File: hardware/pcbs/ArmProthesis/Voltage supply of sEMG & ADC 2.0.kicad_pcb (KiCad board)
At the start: 2 copper layers, 53 x 40 mm, 13 parts, among them U1 TLE2426CD, U2 LT1963AEQ

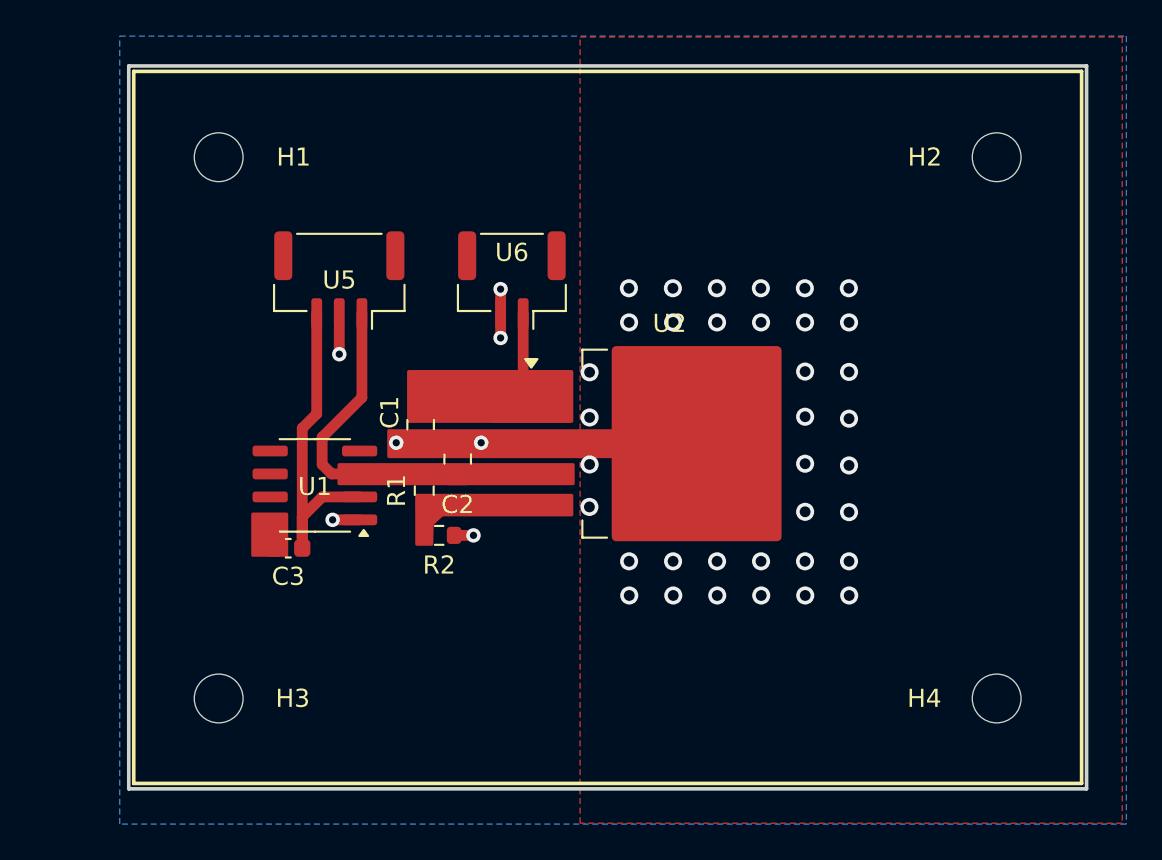
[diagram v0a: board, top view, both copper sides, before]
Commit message: new LDO with a proper rail splitter
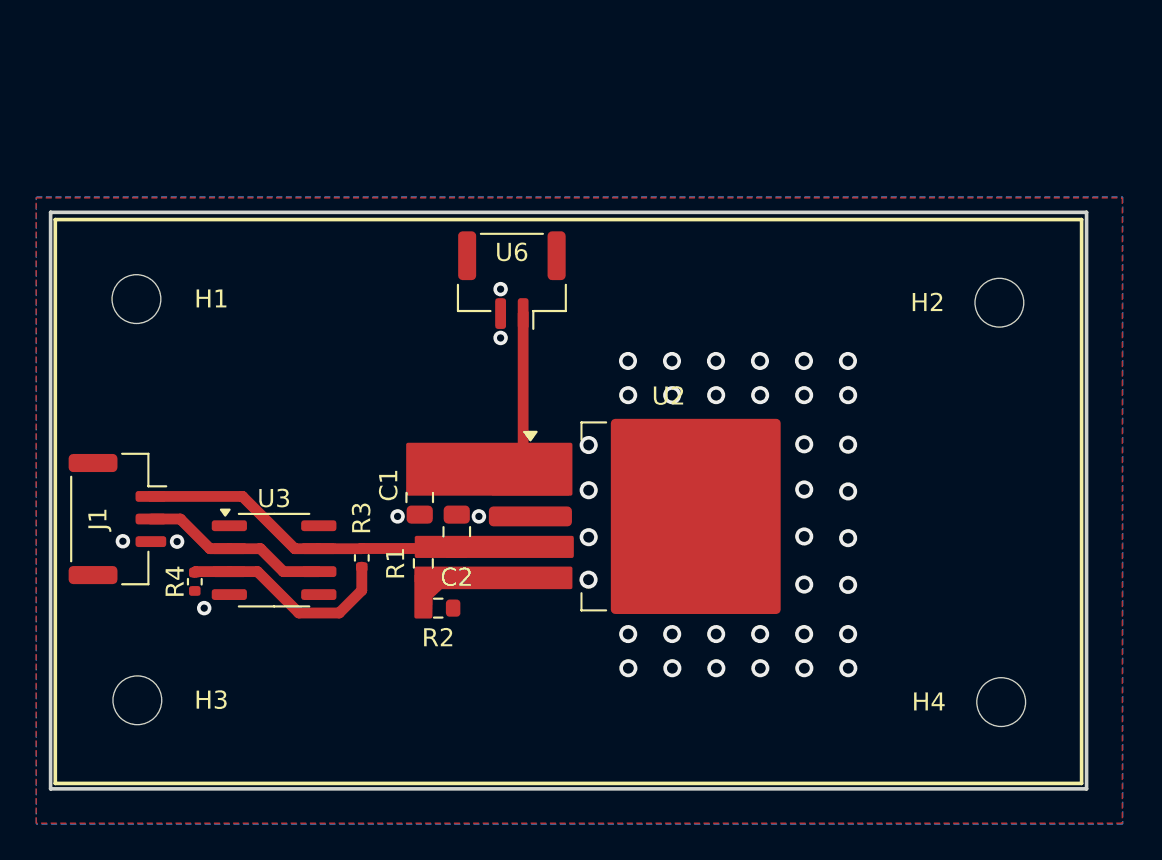
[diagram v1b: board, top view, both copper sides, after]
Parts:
- removed C3: 1uF, Capacitor_SMD:C_0603_1608Metric
- removed U1: TLE2426CD, Package_SO:SOIC-8_3.9x4.9mm_P1.27mm
- removed U5: ~, Connector_JST:JST_GH_SM03B-GHS-TB_1x03-1MP_P1.25mm_Horizontal
- added J1: Conn_01x03, Connector_JST:JST_GH_SM03B-GHS-TB_1x03-1MP_P1.25mm_Horizontal, F.Cu at (98.9, 71.2)
- added R3: 10k, Resistor_SMD:R_0402_1005Metric, F.Cu at (112.4, 73.3)
- added R4: 10k, Resistor_SMD:R_0402_1005Metric, F.Cu at (103.2, 74.6)
- added U3: OPA197xD, Package_SO:SOIC-8_3.9x4.9mm_P1.27mm, F.Cu at (107.6, 73.4)
- moved H1 9.07 mm to (100.0, 59.0)
- moved H2 8.05 mm to (147.7, 59.2)
- moved H3 4.50 mm to (100.0, 81.2)
- moved C2 4.03 mm to (117.7, 71.9)
- moved R1 4.03 mm to (115.8, 73.6)
- moved U2 4.03 mm to (129.4, 71.0)
- moved C1 4.03 mm to (115.6, 70.0)
- moved R2 4.03 mm to (116.7, 76.1)
- moved H4 0.32 mm to (147.8, 81.3)
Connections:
- net /+11.1V renamed 7.4V
- net /+5V renamed 5V
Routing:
- net /VGND: track 18.5 -> 0.00 mm
- net Net-(U3-+): track 0.00 -> 12.0 mm
- net 2.5V: track 0.00 -> 10.5 mm
- net GND: track 6.67 -> 0.00 mm
- net 7.4V: track 3.99 -> 8.63 mm
- net 5V: track 12.7 -> 16.3 mm
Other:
- board size 53 x 40 mm -> 57.3 x 31.9 mm

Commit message: Fixed EMG sensors active band pass filter
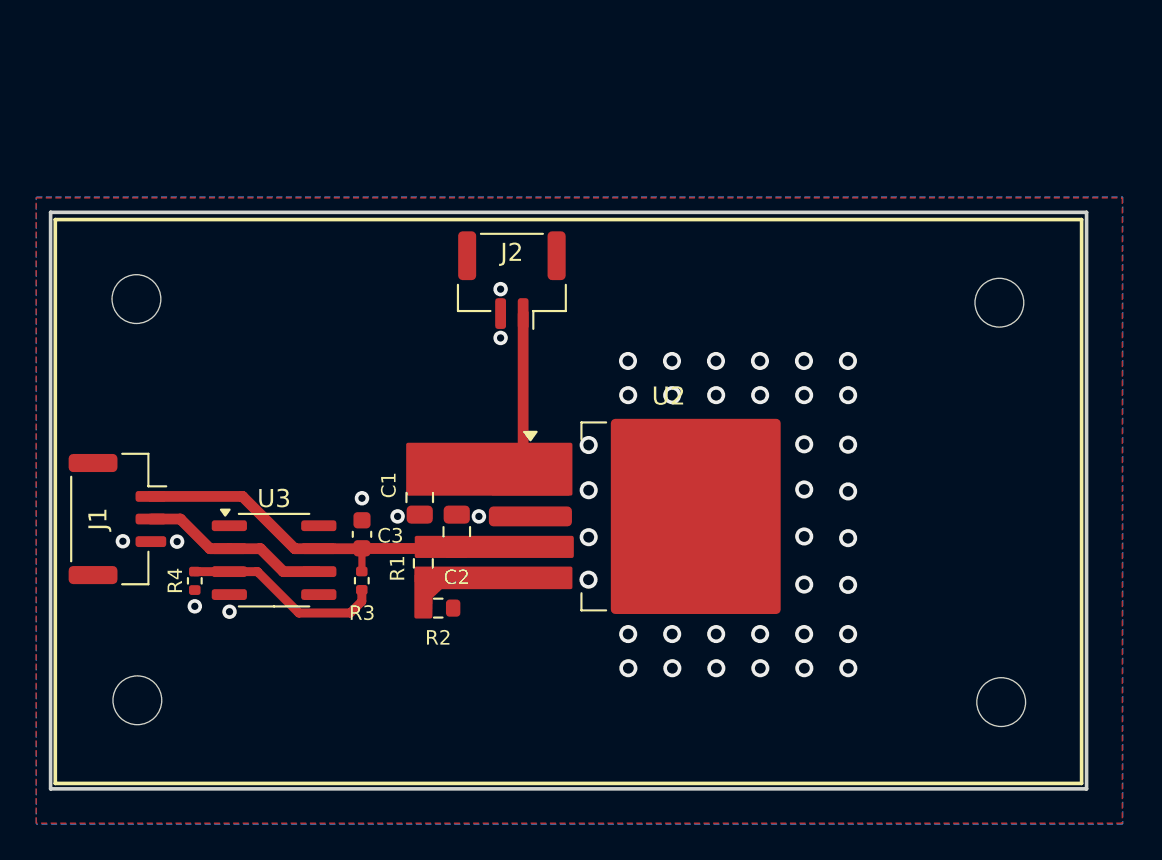
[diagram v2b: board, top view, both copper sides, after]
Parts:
- added C3: 1uF, Capacitor_SMD:C_0603_1608Metric, F.Cu at (112.4, 72.0)
- moved R3 1.26 mm to (112.4, 74.6)
- renumbered U6 to J2
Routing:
- net 5V: track 16.3 -> 17.6 mm
- net Net-(U3-+): track 12.0 -> 11.1 mm
- net GND: vias 43 -> 45

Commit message: Ordered versions
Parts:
- added J3: Conn_01x02, Connector_JST:JST_GH_SM02B-GHS-TB_1x02-1MP_P1.25mm_Horizontal, F.Cu at (113.2, 82.7)
- J2: value ~ -> Conn_01x02
- R1: value 7.25k -> 12.1k
- R2: value 1k -> 3.9k
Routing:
- net 5V: track 17.6 -> 26.7 mm
- net GND: vias 45 -> 47
